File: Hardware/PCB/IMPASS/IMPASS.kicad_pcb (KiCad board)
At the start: 2 copper layers, 80 x 100 mm, 133 parts, among them J1 PUENTE H, J10 SENSORES, J11 SOLENOIDES, J12 POWER, J13 SENSORES, J14 SOLENOIDES, J15 PUENTE H, J16 PUENTE H, J2 POWER, J3 EJE1, J4 EJE2, J5 EJE3, J6 VM, J7 PUENTE H, J8 SOLENOIDES, J9 PROG, Q1 DMN3008SFG, Q10 DMN3008SFG, Q11 DMN3008SFG, Q12 DMN3008SFG, Q13 DMN3008SFG, Q14 DMN3008SFG, Q15 DMN3008SFG, Q16 DMN3008SFG, Q17 DMN3008SFG, Q18 DMN3008SFG, Q19 DMN3008SFG, Q2 DMN3008SFG, Q20 DMN3008SFG, Q21 DMN3008SFG, Q22 DMN3008SFG, Q23 DMN3008SFG, Q24 DMN3008SFG, Q25 2N7002, Q26 2N7002, Q27 2N7002, Q28 2N7002, Q29 2N7002, Q3 DMN3008SFG, Q30 2N7002, Q31 2N7002, Q32 2N7002, Q33 2N7002, Q34 2N7002, Q35 2N7002, Q36 2N7002, Q37 2N7002, Q38 2N7002, Q39 2N7002, Q4 DMN3008SFG, Q40 2N7002, Q41 2N7002, Q42 2N7002, Q43 DMN3008SFG, Q44 DMN3008SFG, Q45 DMN3008SFG, Q46 2N7002, Q47 2N7002, Q48 2N7002, Q5 DMN3008SFG, Q6 DMN3008SFG, Q7 DMN3008SFG, Q8 DMN3008SFG, Q9 DMN3008SFG, SW1 RESET, SW2 BOOT, U1 ESP32-S3-WROOM-1, U10 AMS1117-3.3, U11 AMS1117-5.0, U2 ACS712xLCTR-30A, U3 ACS712xLCTR-30A, U4 ACS712xLCTR-30A, U5 ACS712xLCTR-30A, U6 ACS712xLCTR-30A, U7 ACS712xLCTR-30A, U8 LM75B, U9 LM75B

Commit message: IMPASS schematics update
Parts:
- added C11: 1nF, Capacitor_SMD:C_0603_1608Metric, F.Cu at (128.3, 63.5)
- added C12: 1nF, Capacitor_SMD:C_0603_1608Metric, F.Cu at (143.3, 64.0)
- added C13: 1nF, Capacitor_SMD:C_0603_1608Metric, F.Cu at (153.2, 64.8)
- added C14: 1nF, Capacitor_SMD:C_0603_1608Metric, F.Cu at (157.5, 49.0)
- added C15: 1nF, Capacitor_SMD:C_0603_1608Metric, F.Cu at (133.1, 45.2)
- added C16: 1nF, Capacitor_SMD:C_0603_1608Metric, F.Cu at (120.7, 46.2)
- moved Q23 46.5 mm to (154.0, 41.2), turned to 90 degrees
- moved Q24 44.0 mm to (153.8, 36.9), turned to 180 degrees
- moved Q16 41.3 mm to (126.2, 41.7), turned to -90 degrees
- moved Q14 41.0 mm to (126.2, 37.1), turned to -90 degrees
- moved Q21 40.0 mm to (149.2, 41.1), turned to -90 degrees
- moved Q6 37.9 mm to (138.9, 72.3), turned to 0 degrees
- moved Q22 37.5 mm to (149.4, 36.9)
- moved D3 36.9 mm to (159.5, 61.9), turned to -90 degrees
- moved Q15 35.5 mm to (130.8, 41.5), turned to 0 degrees
- moved Q13 34.9 mm to (131.0, 37.1), turned to 90 degrees
- moved Q5 32.4 mm to (139.0, 68.4)
- moved Q7 31.8 mm to (143.4, 72.4)
- moved Q3 30.1 mm to (126.0, 72.4)
- moved Q1 30.1 mm to (126.0, 67.4)
- moved Q4 30.1 mm to (130.9, 72.4)
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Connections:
- net /Potencia/OUT1_3 renamed out1_3
- J3 pad 1: /Potencia/OUT2_2 -> out1_6
- J3 pad 2: /Potencia/OUT2_1 -> out2_6
- J3 pad 3: /Potencia/OUT1_2 -> out2_5
- J3 pad 4: /Potencia/OUT1_1 -> out1_5
- J4 pad 1: /Potencia/OUT2_4 -> out2_1
- J4 pad 2: /Potencia/OUT1_4 -> out2_2
- J4 pad 3: /Potencia/OUT2_3 -> out1_4
- J5 pad 1: /Potencia/OUT2_6 -> out2_3
- J5 pad 2: /Potencia/OUT1_6 -> out2_4
- J5 pad 3: /Potencia/OUT2_5 -> out1_1
- J5 pad 4: /Potencia/OUT1_5 -> out1_2
- Q1 pad 1: /Potencia/OUT1_1 -> out1_1
- Q1 pad 2: /Potencia/OUT1_1 -> out1_1
- Q1 pad 3: /Potencia/OUT1_1 -> out1_1
- Q10 pad 1: /Potencia/OUT2_3 -> out1_4
- Q10 pad 2: /Potencia/OUT2_3 -> out1_4
- Q10 pad 3: /Potencia/OUT2_3 -> out1_4
- Q12 pad 5: /Potencia/OUT2_3 -> out1_4
- Q13 pad 1: /Potencia/OUT1_4 -> out2_3
- Q13 pad 2: /Potencia/OUT1_4 -> out2_3
- Q13 pad 3: /Potencia/OUT1_4 -> out2_3
- Q14 pad 1: /Potencia/OUT2_4 -> out2_4
- Q14 pad 2: /Potencia/OUT2_4 -> out2_4
- Q14 pad 3: /Potencia/OUT2_4 -> out2_4
- Q15 pad 5: /Potencia/OUT1_4 -> out2_3
- Q16 pad 5: /Potencia/OUT2_4 -> out2_4
- Q17 pad 1: /Potencia/OUT1_5 -> out1_5
- Q17 pad 2: /Potencia/OUT1_5 -> out1_5
- Q17 pad 3: /Potencia/OUT1_5 -> out1_5
- Q18 pad 1: /Potencia/OUT2_5 -> out2_5
- Q18 pad 2: /Potencia/OUT2_5 -> out2_5
- Q18 pad 3: /Potencia/OUT2_5 -> out2_5
- Q19 pad 5: /Potencia/OUT1_5 -> out1_5
- Q2 pad 1: /Potencia/OUT2_1 -> out1_2
- Q2 pad 2: /Potencia/OUT2_1 -> out1_2
- Q2 pad 3: /Potencia/OUT2_1 -> out1_2
- Q20 pad 5: /Potencia/OUT2_5 -> out2_5
- Q21 pad 1: /Potencia/OUT1_6 -> out1_6
- Q21 pad 2: /Potencia/OUT1_6 -> out1_6
- Q21 pad 3: /Potencia/OUT1_6 -> out1_6
- Q22 pad 1: /Potencia/OUT2_6 -> out2_6
- Q22 pad 2: /Potencia/OUT2_6 -> out2_6
- Q22 pad 3: /Potencia/OUT2_6 -> out2_6
- Q23 pad 5: /Potencia/OUT1_6 -> out1_6
- Q24 pad 5: /Potencia/OUT2_6 -> out2_6
- Q3 pad 5: /Potencia/OUT1_1 -> out1_1
- Q4 pad 5: /Potencia/OUT2_1 -> out1_2
- Q44 pad 4: Net-(J11-Pin_1) -> Net-(J11-Pin_3)
- Q45 pad 4: Net-(J11-Pin_3) -> Net-(J11-Pin_1)
- Q5 pad 1: /Potencia/OUT1_2 -> out2_1
- Q5 pad 2: /Potencia/OUT1_2 -> out2_1
- Q5 pad 3: /Potencia/OUT1_2 -> out2_1
- Q6 pad 5: /Potencia/OUT1_2 -> out2_1
- Q7 pad 5: /Potencia/OUT2_2 -> out2_2
- Q8 pad 1: /Potencia/OUT2_2 -> out2_2
- Q8 pad 2: /Potencia/OUT2_2 -> out2_2
- Q8 pad 3: /Potencia/OUT2_2 -> out2_2
- U2 pad 1: /Potencia/OUT1_1 -> out1_1
- U2 pad 2: /Potencia/OUT1_1 -> out1_1
- U2 pad 3: /Potencia/OUT1_2 -> out1_2
- U2 pad 4: /Potencia/OUT1_2 -> out1_2
- U2 pad 6: unconnected-(U2-FILTER-Pad6) -> Net-(U2-FILTER)
- U3 pad 1: /Potencia/OUT2_1 -> out2_1
- U3 pad 2: /Potencia/OUT2_1 -> out2_1
- U3 pad 3: /Potencia/OUT2_2 -> out2_2
- U3 pad 4: /Potencia/OUT2_2 -> out2_2
- U3 pad 6: unconnected-(U3-FILTER-Pad6) -> Net-(U3-FILTER)
- U4 pad 3: /Potencia/OUT1_4 -> out1_4
- U4 pad 4: /Potencia/OUT1_4 -> out1_4
- U4 pad 6: unconnected-(U4-FILTER-Pad6) -> Net-(U4-FILTER)
- U5 pad 1: /Potencia/OUT2_4 -> out2_4
- U5 pad 2: /Potencia/OUT2_4 -> out2_4
- U5 pad 3: /Potencia/OUT2_3 -> out2_3
- U5 pad 4: /Potencia/OUT2_3 -> out2_3
- U6 pad 1: /Potencia/OUT2_5 -> out2_5
- U6 pad 2: /Potencia/OUT2_5 -> out2_5
- U6 pad 3: /Potencia/OUT1_5 -> out1_5
- U6 pad 4: /Potencia/OUT1_5 -> out1_5
- U6 pad 6: unconnected-(U6-FILTER-Pad6) -> Net-(U6-FILTER)
- U7 pad 1: /Potencia/OUT2_6 -> out2_6
- U7 pad 2: /Potencia/OUT2_6 -> out2_6
- U7 pad 3: /Potencia/OUT1_6 -> out1_6
- U7 pad 4: /Potencia/OUT1_6 -> out1_6
- U7 pad 6: unconnected-(U7-FILTER-Pad6) -> Net-(U7-FILTER)
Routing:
- net GND1: track 0.00 -> 245.0 mm, vias 0 -> 10
- net /Potencia/Eje1/Vm: track 0.00 -> 148.2 mm, vias 0 -> 7
- net +5VA: track 0.00 -> 97.1 mm, vias 0 -> 4
- net out1_6: track 0.00 -> 89.8 mm, vias 0 -> 5
- net out2_6: track 0.00 -> 79.2 mm, vias 0 -> 4
- net out1_3: track 0.00 -> 57.5 mm, vias 0 -> 3
- net Net-(D4-K): track 0.00 -> 57.2 mm, vias 0 -> 1
- net out1_4: track 0.00 -> 56.5 mm, vias 0 -> 5
- net out2_5: track 0.00 -> 55.5 mm, vias 0 -> 4
- net Net-(J13-Pin_8): track 0.00 -> 54.3 mm, vias 0 -> 2
- net out2_2: track 0.00 -> 54.1 mm, vias 0 -> 3
- net out2_1: track 0.00 -> 52.7 mm, vias 0 -> 3
- net out1_5: track 0.00 -> 50.1 mm, vias 0 -> 2
- net Net-(J13-Pin_7): track 0.00 -> 49.5 mm, vias 0 -> 2
- net Net-(D5-K): track 0.00 -> 43.5 mm, vias 0 -> 1
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- added copper zone on B.Cu, net GND1
- added copper zone on F.Cu, net GND1

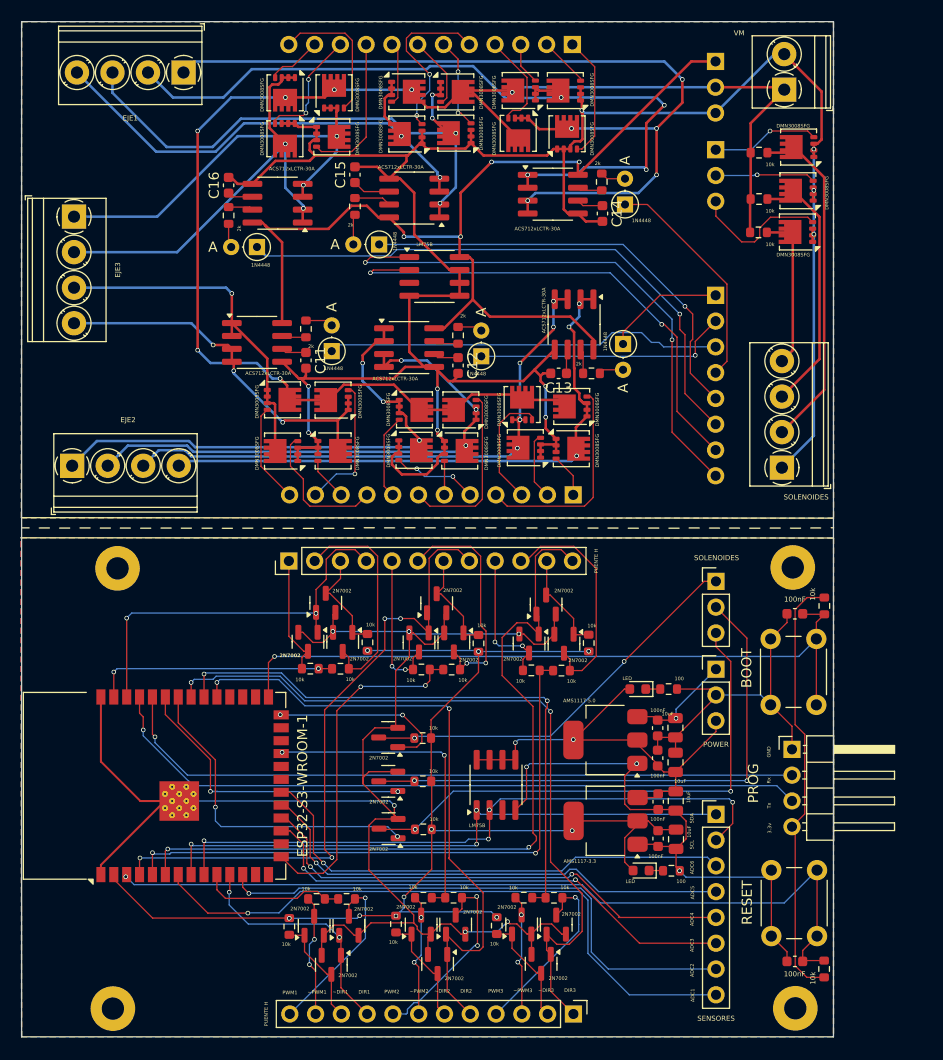
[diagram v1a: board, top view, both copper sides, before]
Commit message: Schematics: Added mpu6050
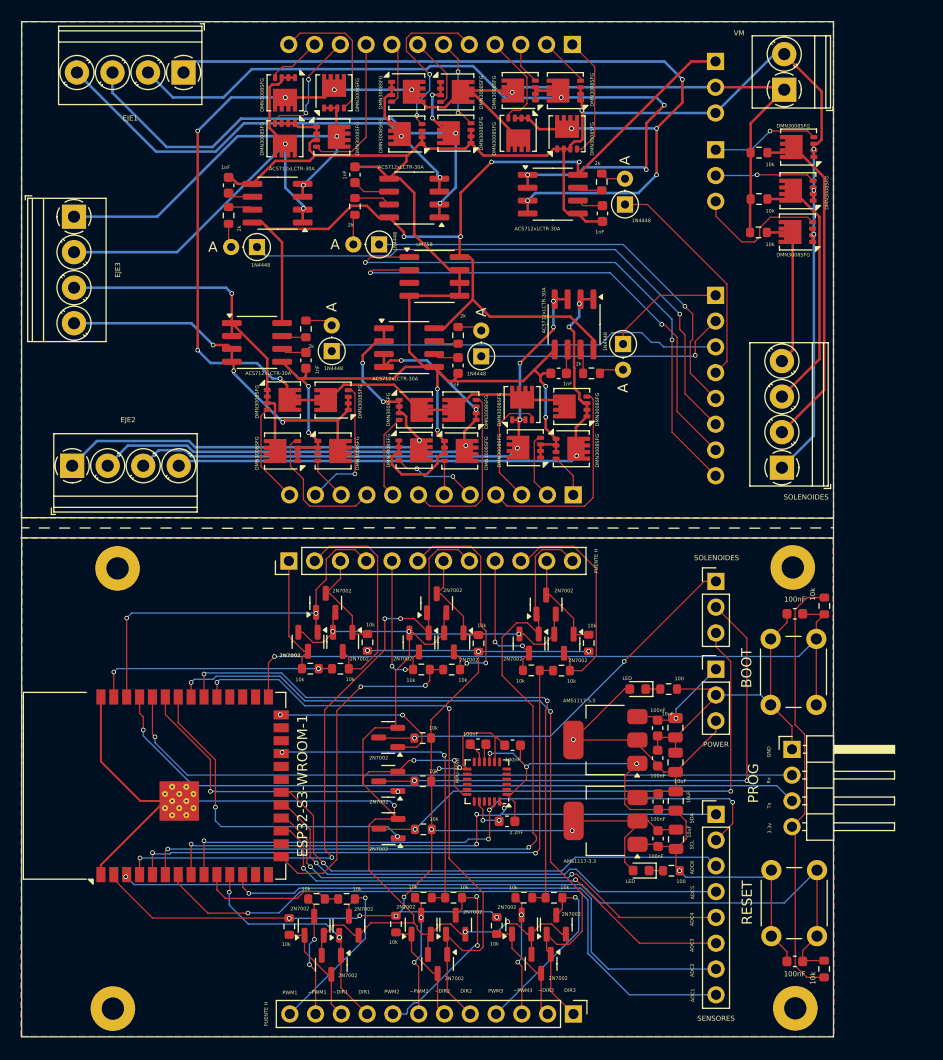
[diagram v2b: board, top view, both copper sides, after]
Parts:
- removed U9: LM75B, Package_SO:SOIC-8_3.9x4.9mm_P1.27mm
- added C17: 100nF, Capacitor_SMD:C_0603_1608Metric, F.Cu at (145.2, 101.3)
- added C18: 2.2nF, Capacitor_SMD:C_0603_1608Metric, F.Cu at (148.1, 108.9)
- added C19: 100nF, Capacitor_SMD:C_0603_1608Metric, F.Cu at (148.6, 101.4)
- added U12: MPU-6050, Sensor_Motion:InvenSense_QFN-24_4x4mm_P0.5mm, F.Cu at (146.1, 105.0)
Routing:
- net GND: track 254.7 -> 276.6 mm, vias 9 -> 12
- net +3.3V: track 166.2 -> 181.2 mm, vias 10 -> 12
- net +5V: track 43.3 -> 31.9 mm, vias 2 -> 1
- net Net-(U12-CPOUT): track 0.00 -> 3.59 mm, vias 0 -> 2
- net Net-(U12-REGOUT): track 0.00 -> 1.81 mm
- net /Logica/SCL: track 63.7 -> 64.8 mm
- net /Logica/SDA: track 58.4 -> 59.5 mm, vias 3 -> 4

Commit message: Restore all the schematics
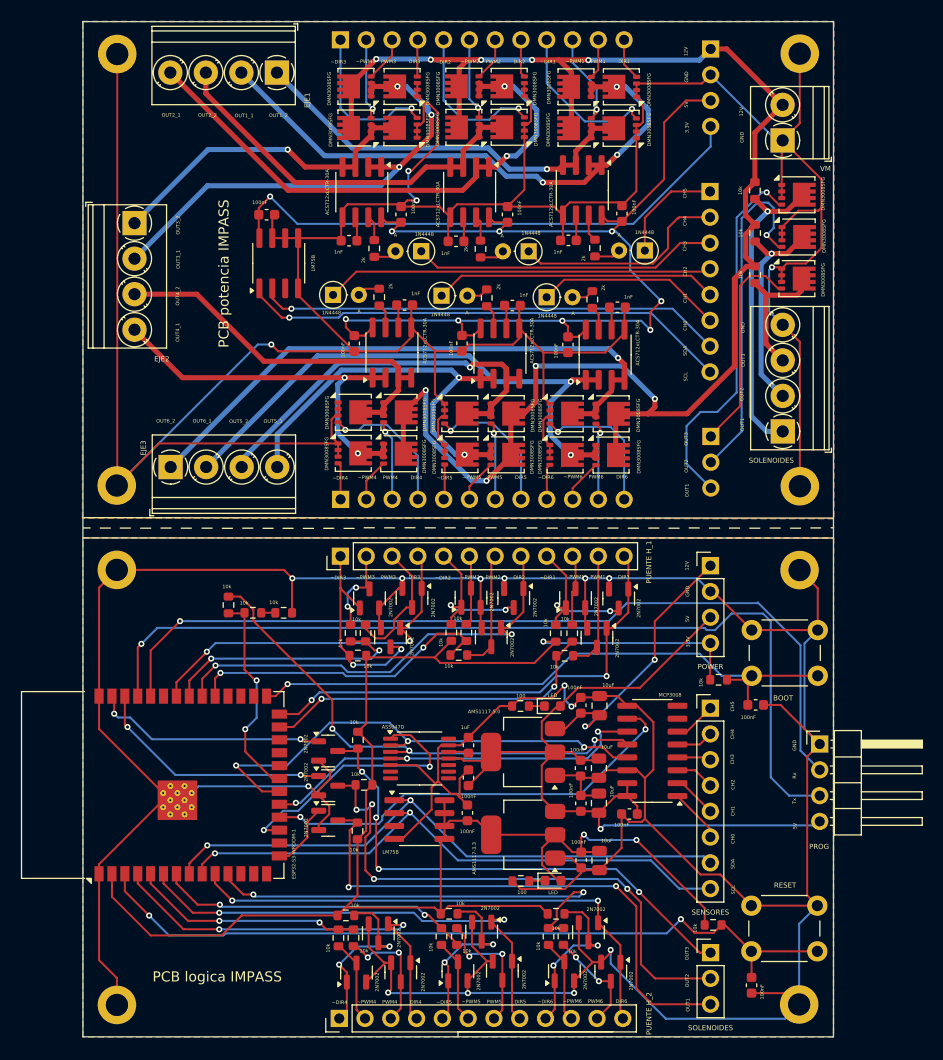
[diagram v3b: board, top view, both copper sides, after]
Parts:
- removed J10, J13: SENSORES, Connector_PinHeader_2.54mm:PinHeader_1x08_P2.54mm_Vertical
- removed J12: POWER, Connector_PinHeader_2.54mm:PinHeader_1x03_P2.54mm_Vertical
- removed J14: SOLENOIDES, TerminalBlock_Phoenix:TerminalBlock_Phoenix_PT-1,5-4-3.5-H_1x04_P3.50mm_Horizontal
- removed J15, J16, J7: PUENTE H, Connector_PinHeader_2.54mm:PinHeader_1x12_P2.54mm_Vertical
- removed J3: EJE1, TerminalBlock_Phoenix:TerminalBlock_Phoenix_PT-1,5-4-3.5-H_1x04_P3.50mm_Horizontal
- removed J4: EJE2, TerminalBlock_Phoenix:TerminalBlock_Phoenix_PT-1,5-4-3.5-H_1x04_P3.50mm_Horizontal
- removed J5: EJE3, TerminalBlock_Phoenix:TerminalBlock_Phoenix_PT-1,5-4-3.5-H_1x04_P3.50mm_Horizontal
- removed J6: VM, TerminalBlock_Phoenix:TerminalBlock_Phoenix_PT-1,5-2-3.5-H_1x02_P3.50mm_Horizontal
- removed J8: SOLENOIDES, Connector_PinHeader_2.54mm:PinHeader_1x03_P2.54mm_Vertical
- removed J9: PROG, Connector_PinHeader_2.54mm:PinHeader_1x04_P2.54mm_Horizontal
- removed Q1, Q2, Q3, Q4, Q5, Q6, Q7, Q8: DMN3008SFG, Package_SON:Diodes_PowerDI3333-8
- removed Q25, Q26, Q27, Q28, Q29, Q30, Q31, Q32, Q33, Q34, Q35, Q36, Q37, Q38, Q39, Q40, Q41, Q42, Q46, Q47, Q48: 2N7002, Package_TO_SOT_SMD:SOT-23
- removed R1, R10, R11, R12, R13, R14, R15, R16, R17, R18, R19, R2, R20, R3, R30, R31, R32, R6, R7, R8, R9: 10k, Resistor_SMD:R_0603_1608Metric
- removed REF** (x4): MountingHole_2.2mm_M2_Pad, MountingHole:MountingHole_2.2mm_M2_Pad
- removed U1: ESP32-S3-WROOM-1, RF_Module:ESP32-S3-WROOM-1
- added C20: 1nF, Capacitor_SMD:C_0603_1608Metric, F.Cu at (132.5, 51.7)
- added C21: 100nF, Capacitor_SMD:C_0603_1608Metric, F.Cu at (133.0, 61.8)
- added C22: 100nF, Capacitor_SMD:C_0603_1608Metric, F.Cu at (143.6, 61.8)
- added C23: 100nF, Capacitor_SMD:C_0603_1608Metric, F.Cu at (154.1, 61.9)
- added C24: 1nF, Capacitor_SMD:C_0603_1608Metric, F.Cu at (138.0, 58.0)
- added C25: 1nF, Capacitor_SMD:C_0603_1608Metric, F.Cu at (159.0, 58.3)
- added C26: 1nF, Capacitor_SMD:C_0603_1608Metric, F.Cu at (148.6, 58.1)
- added C27: 100nF, Capacitor_SMD:C_0603_1608Metric, F.Cu at (160.1, 108.2)
- added H1: MountingHole_Pad, MountingHole:MountingHole_2.2mm_M2_DIN965_Pad, F.Cu at (109.6, 84.1)
- added H2: MountingHole_Pad, MountingHole:MountingHole_2.2mm_M2_DIN965_Pad, F.Cu at (176.9, 84.2)
- added H3: MountingHole_Pad, MountingHole:MountingHole_2.2mm_M2_DIN965_Pad, F.Cu at (176.9, 126.9)
- added H4: MountingHole_Pad, MountingHole:MountingHole_2.2mm_M2_DIN965_Pad, F.Cu at (109.7, 127.0)
- added H5: MountingHole_Pad, MountingHole:MountingHole_2.2mm_M2_DIN965_Pad, F.Cu at (109.7, 33.3)
- added H6: MountingHole_Pad, MountingHole:MountingHole_2.2mm_M2_DIN965_Pad, F.Cu at (176.9, 33.3)
- added H7: MountingHole_Pad, MountingHole:MountingHole_2.2mm_M2_DIN965_Pad, F.Cu at (176.9, 75.9)
- added H8: MountingHole_Pad, MountingHole:MountingHole_2.2mm_M2_DIN965_Pad, F.Cu at (109.6, 75.8)
- added J17: PUENTE H_1, Connector_PinHeader_2.54mm:PinHeader_1x12_P2.54mm_Vertical, F.Cu at (131.7, 82.8)
- added J18: PUENTE H_2, Connector_PinHeader_2.54mm:PinHeader_1x12_P2.54mm_Vertical, F.Cu at (131.6, 128.3)
- added J19: SOLENOIDES, Connector_PinHeader_2.54mm:PinHeader_1x03_P2.54mm_Vertical, F.Cu at (168.1, 121.8)
- added J20: SENSORES, Connector_PinHeader_2.54mm:PinHeader_1x08_P2.54mm_Vertical, F.Cu at (168.1, 97.8)
- added J21: PROG, Connector_PinHeader_2.54mm:PinHeader_1x04_P2.54mm_Horizontal, F.Cu at (178.9, 101.3)
- added J22: VM, TerminalBlock_Phoenix:TerminalBlock_Phoenix_PT-1,5-2-3.5-H_1x02_P3.50mm_Horizontal, F.Cu at (175.2, 41.8)
- added J23: EJE1, TerminalBlock_Phoenix:TerminalBlock_Phoenix_PT-1,5-4-3.5-H_1x04_P3.50mm_Horizontal, F.Cu at (125.4, 35.1)
- added J24: EJE2, TerminalBlock_Phoenix:TerminalBlock_Phoenix_PT-1,5-4-3.5-H_1x04_P3.50mm_Horizontal, F.Cu at (111.4, 50.0)
- added J25: EJE3, TerminalBlock_Phoenix:TerminalBlock_Phoenix_PT-1,5-4-3.5-H_1x04_P3.50mm_Horizontal, F.Cu at (114.9, 74.0)
- added J26: SOLENOIDES, TerminalBlock_Phoenix:TerminalBlock_Phoenix_PT-1,5-4-3.5-H_1x04_P3.50mm_Horizontal, F.Cu at (175.2, 70.5)
- added J27: PUENTE H, Connector_PinHeader_2.54mm:PinHeader_1x12_P2.54mm_Vertical, B.Cu at (131.7, 77.2)
- added J28: PUENTE H, Connector_PinHeader_2.54mm:PinHeader_1x12_P2.54mm_Vertical, B.Cu at (131.7, 31.9)
- added J29: SENSORES, Connector_PinHeader_2.54mm:PinHeader_1x08_P2.54mm_Vertical, B.Cu at (168.1, 46.9)
- added Q49: 2N7002, Package_TO_SOT_SMD:SOT-23, F.Cu at (159.1, 87.0)
- added Q50: 2N7002, Package_TO_SOT_SMD:SOT-23, F.Cu at (154.8, 86.9)
- added Q51: 2N7002, Package_TO_SOT_SMD:SOT-23, F.Cu at (156.9, 90.8)
- added Q52: 2N7002, Package_TO_SOT_SMD:SOT-23, F.Cu at (148.7, 86.9)
- added Q53: 2N7002, Package_TO_SOT_SMD:SOT-23, F.Cu at (144.5, 86.9)
- added Q54: 2N7002, Package_TO_SOT_SMD:SOT-23, F.Cu at (146.5, 90.8)
- added Q55: 2N7002, Package_TO_SOT_SMD:SOT-23, F.Cu at (136.6, 90.8)
- added Q56: 2N7002, Package_TO_SOT_SMD:SOT-23, F.Cu at (134.5, 86.9)
- added Q57: 2N7002, Package_TO_SOT_SMD:SOT-23, F.Cu at (138.7, 86.9)
- added Q58: 2N7002, Package_TO_SOT_SMD:SOT-23, F.Cu at (135.4, 119.9)
- added Q59: 2N7002, Package_TO_SOT_SMD:SOT-23, F.Cu at (145.6, 119.8)
- added Q60: 2N7002, Package_TO_SOT_SMD:SOT-23, F.Cu at (156.1, 119.8)
- added Q61: 2N7002, Package_TO_SOT_SMD:SOT-23, F.Cu at (133.2, 123.8)
- added Q62: 2N7002, Package_TO_SOT_SMD:SOT-23, F.Cu at (143.2, 123.7)
- added Q63: 2N7002, Package_TO_SOT_SMD:SOT-23, F.Cu at (153.7, 123.7)
- added Q64: 2N7002, Package_TO_SOT_SMD:SOT-23, F.Cu at (137.6, 123.8)
- added Q65: 2N7002, Package_TO_SOT_SMD:SOT-23, F.Cu at (147.6, 123.6)
- added Q66: 2N7002, Package_TO_SOT_SMD:SOT-23, F.Cu at (158.3, 123.7)
- added Q67: 2N7002, Package_TO_SOT_SMD:SOT-23, F.Cu at (130.5, 108.8)
- added Q68: 2N7002, Package_TO_SOT_SMD:SOT-23, F.Cu at (130.5, 105.4)
- added Q69: 2N7002, Package_TO_SOT_SMD:SOT-23, F.Cu at (130.5, 102.0)
- added Q70: DMN3008SFG, Package_SON:Diodes_PowerDI3333-8, F.Cu at (154.9, 36.5)
- added Q71: DMN3008SFG, Package_SON:Diodes_PowerDI3333-8, F.Cu at (159.3, 36.5)
- added Q72: DMN3008SFG, Package_SON:Diodes_PowerDI3333-8, F.Cu at (143.8, 36.5)
- added Q73: DMN3008SFG, Package_SON:Diodes_PowerDI3333-8, F.Cu at (148.3, 36.5)
- added Q74: DMN3008SFG, Package_SON:Diodes_PowerDI3333-8, F.Cu at (154.9, 40.6)
- added Q75: DMN3008SFG, Package_SON:Diodes_PowerDI3333-8, F.Cu at (159.3, 40.6)
- added Q76: DMN3008SFG, Package_SON:Diodes_PowerDI3333-8, F.Cu at (143.8, 40.5)
- added Q77: DMN3008SFG, Package_SON:Diodes_PowerDI3333-8, F.Cu at (148.3, 40.5)
- added R35: 10k, Resistor_SMD:R_0603_1608Metric, F.Cu at (152.9, 90.4)
- added R36: 10k, Resistor_SMD:R_0603_1608Metric, F.Cu at (154.5, 90.4)
- added R37: 10k, Resistor_SMD:R_0603_1608Metric, F.Cu at (153.8, 92.6)
- added R38: 10k, Resistor_SMD:R_0603_1608Metric, F.Cu at (142.6, 90.3)
- added R39: 10k, Resistor_SMD:R_0603_1608Metric, F.Cu at (144.1, 90.3)
- added R40: 10k, Resistor_SMD:R_0603_1608Metric, F.Cu at (143.3, 92.5)
- added R41: 10k, Resistor_SMD:R_0603_1608Metric, F.Cu at (133.4, 92.6)
- added R42: 10k, Resistor_SMD:R_0603_1608Metric, F.Cu at (132.7, 90.3)
- added R43: 10k, Resistor_SMD:R_0603_1608Metric, F.Cu at (134.2, 90.3)
- added R44: 10k, Resistor_SMD:R_0603_1608Metric, F.Cu at (132.2, 118.2)
- added R45: 10k, Resistor_SMD:R_0603_1608Metric, F.Cu at (142.4, 118.0)
- added R46: 10k, Resistor_SMD:R_0603_1608Metric, F.Cu at (152.9, 118.0)
- added R47: 10k, Resistor_SMD:R_0603_1608Metric, F.Cu at (131.5, 120.4)
- added R48: 10k, Resistor_SMD:R_0603_1608Metric, F.Cu at (141.6, 120.2)
- added R49: 10k, Resistor_SMD:R_0603_1608Metric, F.Cu at (152.2, 120.2)
- added R50: 10k, Resistor_SMD:R_0603_1608Metric, F.Cu at (132.9, 120.4)
- added R51: 10k, Resistor_SMD:R_0603_1608Metric, F.Cu at (143.1, 120.2)
- added R52: 10k, Resistor_SMD:R_0603_1608Metric, F.Cu at (153.6, 120.2)
- added R53: 10k, Resistor_SMD:R_0603_1608Metric, F.Cu at (133.3, 109.8)
- added R54: 10k, Resistor_SMD:R_0603_1608Metric, F.Cu at (134.0, 105.3)
- added R55: 10k, Resistor_SMD:R_0603_1608Metric, F.Cu at (133.4, 100.9)
- added R56: 10k, Resistor_SMD:R_0603_1608Metric, F.Cu at (123.0, 88.4)
- added R57: 10k, Resistor_SMD:R_0603_1608Metric, F.Cu at (126.1, 88.4)
- added R58: 10k, Resistor_SMD:R_0603_1608Metric, F.Cu at (120.6, 87.6)
- added U13: MCP3008, Package_SO:SOIC-16_3.9x9.9mm_P1.27mm, F.Cu at (162.4, 102.0)
- added U14: ESP32-S3-WROOM-1, RF_Module:ESP32-S3-WROOM-1, F.Cu at (113.2, 105.3)
- added U9: LM75B, Package_SO:SOIC-8_3.9x4.9mm_P1.27mm, F.Cu at (139.4, 108.7)
- C11, C12, C13, C14: value 1nF -> 100nF
- C18: value 2.2nF -> 1uF
- C4, C8: value 100nF -> 10uF; footprint Capacitor_SMD:C_0603_1608Metric -> Capacitor_SMD:C_0805_2012Metric
- C5, C9: value 10uF -> 100nF; footprint Capacitor_SMD:C_0805_2012Metric -> Capacitor_SMD:C_0603_1608Metric
- J1: value PUENTE H -> POWER; footprint Connector_PinHeader_2.54mm:PinHeader_1x12_P2.54mm_Vertical -> Connector_PinHeader_2.54mm:PinHeader_1x04_P2.54mm_Vertical
- J2: footprint Connector_PinHeader_2.54mm:PinHeader_1x03_P2.54mm_Vertical -> Connector_PinHeader_2.54mm:PinHeader_1x04_P2.54mm_Vertical
- U12: value MPU-6050 -> AS5047D; footprint Sensor_Motion:InvenSense_QFN-24_4x4mm_P0.5mm -> Package_SO:TSSOP-14_4.4x5mm_P0.65mm
- U2: value ACS712xLCTR-30A -> LM75B
- U8: value LM75B -> ACS712xLCTR-30A
- moved J1 41.5 mm to (168.1, 83.7), turned to 0 degrees
- moved Q11 39.4 mm to (137.7, 36.5), turned to 180 degrees
- moved Q9 38.0 mm to (133.2, 36.5)
- moved Q17 37.1 mm to (148.0, 72.8)
- moved Q13 36.1 mm to (137.4, 72.7), turned to 0 degrees
- moved C11 34.3 mm to (159.4, 49.0), turned to 90 degrees
- moved Q12 33.8 mm to (137.7, 40.6)
- moved Q14 33.4 mm to (137.4, 68.6), turned to 0 degrees
- moved Q22 33.1 mm to (158.3, 68.8), turned to 0 degrees
- moved C14 33.1 mm to (124.4, 49.1), turned to 0 degrees
- moved Q21 33.0 mm to (158.3, 72.8), turned to 0 degrees
- moved D1 32.4 mm to (161.7, 52.7), turned to 180 degrees
- moved Q18 32.1 mm to (148.0, 68.7)
- moved Q19 32.0 mm to (143.4, 72.8), turned to 0 degrees
- moved Q24 31.8 mm to (153.8, 68.7), turned to 0 degrees
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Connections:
- net /Logica/BOOT renamed /Placa_logica/BOOT
- net /Logica/RESET renamed /Placa_logica/RESET
- net /Potencia/Solenoides/OUT1 renamed /Placa_potencia/Solenoides/OUT1
- net /Potencia/Solenoides/OUT2 renamed /Placa_potencia/Solenoides/OUT2
- net /Potencia/Solenoides/OUT3 renamed /Placa_potencia/Solenoides/OUT3
- net Net-(J11-Pin_1) renamed /Placa_potencia/Solenoides/INPUT_1
- net Net-(J11-Pin_2) renamed /Placa_potencia/Solenoides/INPUT_2
- net Net-(J11-Pin_3) renamed /Placa_potencia/Solenoides/INPUT_3
- net out2_1 renamed /Placa_potencia/Eje1/OUT1_1
- net out2_2 renamed /Placa_potencia/Eje1/OUT1_2
- C10 pad 1: +3.3V -> +5V
- C11 pad 1: Net-(U2-FILTER) -> /Placa_potencia/Sensores_potencia/5V
- C12 pad 1: Net-(U3-FILTER) -> /Placa_potencia/Sensores_potencia/5V
- C13 pad 1: Net-(U4-FILTER) -> /Placa_potencia/Sensores_potencia/5V
- C14 pad 1: Net-(U7-FILTER) -> /Placa_potencia/Sensores_potencia/3.3V
- C15 pad 1: Net-(U6-FILTER) -> Net-(U3-FILTER)
- C16 pad 1: unconnected-(C16-Pad1) -> Net-(U4-FILTER)
- C17 pad 1: Net-(U12-REGOUT) -> +3.3V
- C18 pad 1: Net-(U12-CPOUT) -> Net-(U12-VDD3V3)
- C19 pad 1: +3.3V -> +5V
- C3 pad 1: Net-(J12-Pin_1) -> +5V
- C4 pad 1: Net-(J12-Pin_1) -> /12v
- C6 pad 1: +5V -> /12v
- C7 pad 1: +5V -> +3.3V
- D1 pad 1: Net-(D1-K) -> /Placa_potencia/Sensores_potencia/I_1
- D2 pad 1: Net-(D2-K) -> /Placa_potencia/Sensores_potencia/I_2
- D3 pad 1: Net-(D3-K) -> /Placa_potencia/Sensores_potencia/I_3
- D4 pad 1: Net-(D4-K) -> /Placa_potencia/Sensores_potencia/I_4
- D5 pad 1: Net-(D5-K) -> /Placa_potencia/Sensores_potencia/I_5
- D6 pad 1: Net-(D6-K) -> /Placa_potencia/Sensores_potencia/I_6
- D7 pad 2: +5V -> +3.3V
- D8 pad 2: +3.3V -> +5V
- J1 pad 1: /Logica/PWM4 -> /12v
- J1 pad 2: /Logica/~PWM4 -> GND
- J1 pad 3: /Logica/~DIR4 -> +5V
- J1 pad 4: /Logica/DIR4 -> +3.3V
- J2 pad 1: +5VA -> 12v
- J2 pad 2: /Potencia/Eje1/Vm -> GND1
- J2 pad 3: GND1 -> /Placa_potencia/Sensores_potencia/5V
- Q10 pad 1: out1_4 -> /Placa_potencia/Eje2/OUT3_2
- Q10 pad 2: out1_4 -> /Placa_potencia/Eje2/OUT3_2
- Q10 pad 3: out1_4 -> /Placa_potencia/Eje2/OUT3_2
- Q10 pad 4: /Potencia/~PWM3 -> /Placa_potencia/Eje2/~PWM3
- Q10 pad 5: /Potencia/Eje1/Vm -> 12v
- Q11 pad 4: /Potencia/DIR3 -> /Placa_potencia/Eje2/DIR3
- Q11 pad 5: out1_3 -> /Placa_potencia/Eje2/OUT3_1
- Q12 pad 4: /Potencia/~DIR3 -> /Placa_potencia/Eje2/~DIR3
- Q12 pad 5: out1_4 -> /Placa_potencia/Eje2/OUT3_2
- Q13 pad 1: out2_3 -> /Placa_potencia/Eje2/OUT4_1
- Q13 pad 2: out2_3 -> /Placa_potencia/Eje2/OUT4_1
- Q13 pad 3: out2_3 -> /Placa_potencia/Eje2/OUT4_1
- Q13 pad 4: /Potencia/PWM4 -> /Placa_potencia/Eje2/PWM4
- Q13 pad 5: /Potencia/Eje1/Vm -> 12v
- Q14 pad 1: out2_4 -> /Placa_potencia/Eje2/OUT4_2
- Q14 pad 2: out2_4 -> /Placa_potencia/Eje2/OUT4_2
- Q14 pad 3: out2_4 -> /Placa_potencia/Eje2/OUT4_2
- Q14 pad 4: /Potencia/~PWM4 -> /Placa_potencia/Eje2/~PWM4
- Q14 pad 5: /Potencia/Eje1/Vm -> 12v
- Q15 pad 4: /Potencia/DIR4 -> /Placa_potencia/Eje2/DIR4
- Q15 pad 5: out2_3 -> /Placa_potencia/Eje2/OUT4_1
- Q16 pad 4: /Potencia/~DIR4 -> /Placa_potencia/Eje2/~DIR4
- Q16 pad 5: out2_4 -> /Placa_potencia/Eje2/OUT4_2
- Q17 pad 1: out1_5 -> /Placa_potencia/Eje3/OUT5_1
- Q17 pad 2: out1_5 -> /Placa_potencia/Eje3/OUT5_1
- Q17 pad 3: out1_5 -> /Placa_potencia/Eje3/OUT5_1
- Q17 pad 4: /Potencia/PWM5 -> /Placa_potencia/Eje3/PWM5
- Q17 pad 5: /Potencia/Eje1/Vm -> 12v
- Q18 pad 1: out2_5 -> /Placa_potencia/Eje3/OUT5_2
- Q18 pad 2: out2_5 -> /Placa_potencia/Eje3/OUT5_2
- Q18 pad 3: out2_5 -> /Placa_potencia/Eje3/OUT5_2
- Q18 pad 4: /Potencia/~PWM5 -> /Placa_potencia/Eje3/~PWM5
- Q18 pad 5: /Potencia/Eje1/Vm -> 12v
- Q19 pad 4: /Potencia/DIR5 -> /Placa_potencia/Eje3/DIR5
- Q19 pad 5: out1_5 -> /Placa_potencia/Eje3/OUT5_1
- Q20 pad 4: /Potencia/~DIR5 -> /Placa_potencia/Eje3/~DIR5
- Q20 pad 5: out2_5 -> /Placa_potencia/Eje3/OUT5_2
- Q21 pad 1: out1_6 -> /Placa_potencia/Eje3/OUT6_1
- Q21 pad 2: out1_6 -> /Placa_potencia/Eje3/OUT6_1
- Q21 pad 3: out1_6 -> /Placa_potencia/Eje3/OUT6_1
- Q21 pad 4: /Potencia/PWM6 -> /Placa_potencia/Eje3/PWM6
- Q21 pad 5: /Potencia/Eje1/Vm -> 12v
- Q22 pad 1: out2_6 -> /Placa_potencia/Eje3/OUT6_2
- Q22 pad 2: out2_6 -> /Placa_potencia/Eje3/OUT6_2
- Q22 pad 3: out2_6 -> /Placa_potencia/Eje3/OUT6_2
- Q22 pad 4: /Potencia/~PWM6 -> /Placa_potencia/Eje3/~PWM6
- Q22 pad 5: /Potencia/Eje1/Vm -> 12v
- Q23 pad 4: /Potencia/DIR6 -> /Placa_potencia/Eje3/DIR6
- Q23 pad 5: out1_6 -> /Placa_potencia/Eje3/OUT6_1
- Q24 pad 4: /Potencia/~DIR6 -> /Placa_potencia/Eje3/~DIR6
- Q24 pad 5: out2_6 -> /Placa_potencia/Eje3/OUT6_2
- Q9 pad 1: out1_3 -> /Placa_potencia/Eje2/OUT3_1
- Q9 pad 2: out1_3 -> /Placa_potencia/Eje2/OUT3_1
- Q9 pad 3: out1_3 -> /Placa_potencia/Eje2/OUT3_1
- Q9 pad 4: /Potencia/PWM3 -> /Placa_potencia/Eje2/PWM3
- Q9 pad 5: /Potencia/Eje1/Vm -> 12v
- R21 pad 1: Net-(U2-VIOUT) -> Net-(U3-VIOUT)
- R22 pad 1: Net-(U3-VIOUT) -> Net-(U4-VIOUT)
- R23 pad 1: Net-(U4-VIOUT) -> Net-(U5-VIOUT)
- R24 pad 1: Net-(U5-VIOUT) -> Net-(U6-VIOUT)
- R25 pad 1: Net-(U6-VIOUT) -> Net-(U7-VIOUT)
- R26 pad 1: Net-(U7-VIOUT) -> Net-(U8-VIOUT)
- R27 pad 1: /Potencia/Eje1/Vm -> 12v
- R28 pad 1: /Potencia/Eje1/Vm -> 12v
- R29 pad 1: /Potencia/Eje1/Vm -> 12v
- U11 pad 3: Net-(J12-Pin_1) -> /12v
- U12 pad 1: GND -> cs_INC
- U12 pad 10: Net-(U12-REGOUT) -> unconnected-(U12-U-Pad10)
- U12 pad 11: GND -> +5V
- U12 pad 12: unconnected-(U12-INT-Pad12) -> Net-(U12-VDD3V3)
- U12 pad 13: +3.3V -> GND
- U12 pad 2: unconnected-(U12-NC-Pad2) -> SCK
- U12 pad 3: unconnected-(U12-NC-Pad3) -> MISO
- U12 pad 4: unconnected-(U12-NC-Pad4) -> MOSI
- U12 pad 5: unconnected-(U12-NC-Pad5) -> GND
- U12 pad 8: +3.3V -> unconnected-(U12-W/PWM-Pad8)
- U12 pad 9: GND -> unconnected-(U12-V-Pad9)
- U2 pad 1: out1_1 -> /Placa_potencia/Sensores_potencia/SDA
- U2 pad 2: out1_1 -> /Placa_potencia/Sensores_potencia/SCL
- U2 pad 3: out1_2 -> unconnected-(U2-O.S.-Pad3)
- U2 pad 4: out1_2 -> GND1
- U2 pad 6: Net-(U2-FILTER) -> GND1
- U2 pad 7: Net-(U2-VIOUT) -> GND1
- U2 pad 8: +5VA -> /Placa_potencia/Sensores_potencia/3.3V
- U3 pad 8: +5VA -> /Placa_potencia/Sensores_potencia/5V
- U4 pad 1: out1_3 -> /Placa_potencia/Eje1/OUT2_1
- U4 pad 2: out1_3 -> /Placa_potencia/Eje1/OUT2_1
- U4 pad 3: out1_4 -> /Placa_potencia/Eje1/OUT2_2
- U4 pad 4: out1_4 -> /Placa_potencia/Eje1/OUT2_2
- U4 pad 8: +5VA -> /Placa_potencia/Sensores_potencia/5V
- U5 pad 1: out2_4 -> /Placa_potencia/Eje2/OUT3_1
- U5 pad 2: out2_4 -> /Placa_potencia/Eje2/OUT3_1
- U5 pad 3: out2_3 -> /Placa_potencia/Eje2/OUT3_2
- U5 pad 4: out2_3 -> /Placa_potencia/Eje2/OUT3_2
- U5 pad 6: unconnected-(U5-FILTER-Pad6) -> Net-(U5-FILTER)
- U5 pad 8: +5VA -> /Placa_potencia/Sensores_potencia/5V
- U6 pad 1: out2_5 -> /Placa_potencia/Eje2/OUT4_1
- U6 pad 2: out2_5 -> /Placa_potencia/Eje2/OUT4_1
- U6 pad 3: out1_5 -> /Placa_potencia/Eje2/OUT4_2
- U6 pad 4: out1_5 -> /Placa_potencia/Eje2/OUT4_2
- U6 pad 8: +5VA -> /Placa_potencia/Sensores_potencia/5V
- U7 pad 1: out2_6 -> /Placa_potencia/Eje3/OUT5_1
- U7 pad 2: out2_6 -> /Placa_potencia/Eje3/OUT5_1
- U7 pad 3: out1_6 -> /Placa_potencia/Eje3/OUT5_2
- U7 pad 4: out1_6 -> /Placa_potencia/Eje3/OUT5_2
- U7 pad 8: +5VA -> /Placa_potencia/Sensores_potencia/5V
- U8 pad 1: Net-(J13-Pin_8) -> /Placa_potencia/Eje3/OUT6_1
- U8 pad 2: Net-(J13-Pin_7) -> /Placa_potencia/Eje3/OUT6_1
- U8 pad 3: unconnected-(U8-O.S.-Pad3) -> /Placa_potencia/Eje3/OUT6_2
- U8 pad 4: GND1 -> /Placa_potencia/Eje3/OUT6_2
- U8 pad 6: GND1 -> Net-(U8-FILTER)
- U8 pad 7: GND1 -> Net-(U8-VIOUT)
- U8 pad 8: +5VA -> /Placa_potencia/Sensores_potencia/5V
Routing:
- net 12v: track 0.00 -> 160.7 mm, vias 0 -> 9
- net /Potencia/Eje1/Vm: track 148.2 -> 0.00 mm, vias 7 -> 0
- net GND: track 276.6 -> 413.3 mm, vias 12 -> 13
- net GND1: track 245.0 -> 353.2 mm, vias 10 -> 4
- net /Placa_potencia/Sensores_potencia/5V: track 0.00 -> 103.8 mm, vias 0 -> 8
- net +5VA: track 97.1 -> 0.00 mm, vias 4 -> 0
- net /Placa_logica/Tx: track 0.00 -> 90.0 mm, vias 0 -> 1
- net out1_6: track 89.8 -> 0.00 mm, vias 5 -> 0
- net /Placa_logica/Rx: track 0.00 -> 85.3 mm, vias 0 -> 1
- net out2_6: track 79.2 -> 0.00 mm, vias 4 -> 0
- net /Logica/DIR6: track 77.6 -> 0.00 mm, vias 2 -> 0
- net /Logica/DIR3: track 74.9 -> 0.00 mm, vias 2 -> 0
- net /Logica/TX: track 70.6 -> 0.00 mm, vias 1 -> 0
- net /Logica/RX: track 68.7 -> 0.00 mm, vias 1 -> 0
- net /Logica/SCL: track 64.8 -> 0.00 mm, vias 4 -> 0
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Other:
- board size 80 x 100 mm -> 73.9 x 100 mm
- board text added: "12V"
- board text added: "3.3V"
- board text added: "5V"
- board text added: "CH0"
- board text added: "CH1"
- board text added: "CH2"
- board text added: "CH3"
- board text added: "CH4"
- board text added: "CH5"
- board text added: "DIR4"
- board text added: "DIR5"
- board text added: "DIR6"
- board text added: "OUT1"
- board text added: "OUT1_1"
- board text added: "OUT1_2"
- board text added: "OUT2"
- board text added: "OUT2_1"
- board text added: "OUT2_2"
- board text added: "OUT3"
- board text added: "OUT3_1"
- board text added: "OUT3_2"
- board text added: "OUT4_1"
- board text added: "OUT4_2"
- board text added: "OUT5_1"
- board text added: "OUT5_2"
- board text added: "OUT6_1"
- board text added: "OUT6_2"
- board text added: "PCB logica IMPASS"
- board text added: "PCB potencia IMPASS"
- board text added: "PWM4"
- board text added: "PWM5"
- board text added: "PWM6"
- board text added: "~DIR4"
- board text added: "~DIR5"
- board text added: "~DIR6"
- board text added: "~PWM4"
- board text added: "~PWM5"
- board text added: "~PWM6"
- board text removed: "3.3v"
- board text removed: "ADC1"
- board text removed: "ADC2"
- board text removed: "ADC3"
- board text removed: "ADC4"
- board text removed: "ADC5"
- board text removed: "ADC6"
